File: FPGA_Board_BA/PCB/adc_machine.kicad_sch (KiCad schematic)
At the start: 15 parts, among them U11 LTC2320-16_CMOS

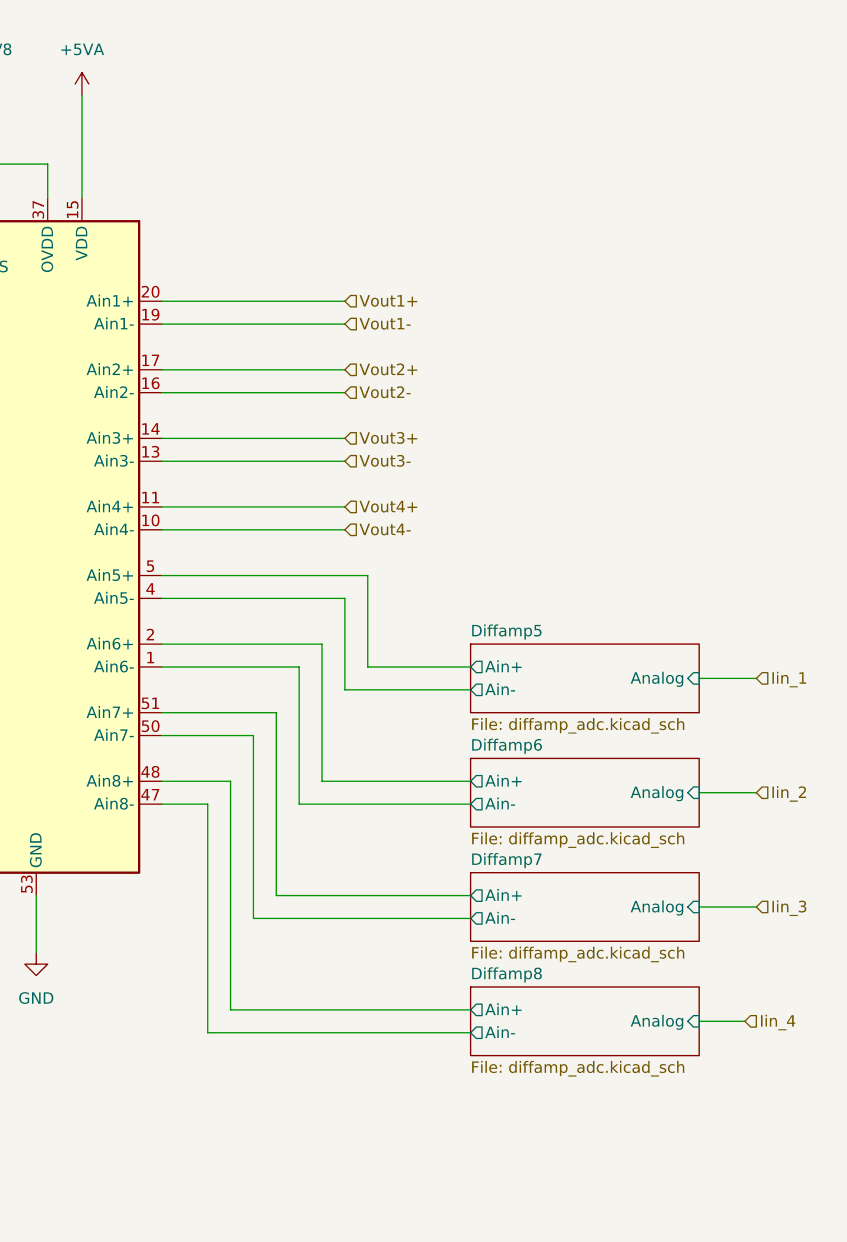
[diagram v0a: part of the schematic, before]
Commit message: started power DCDC layout
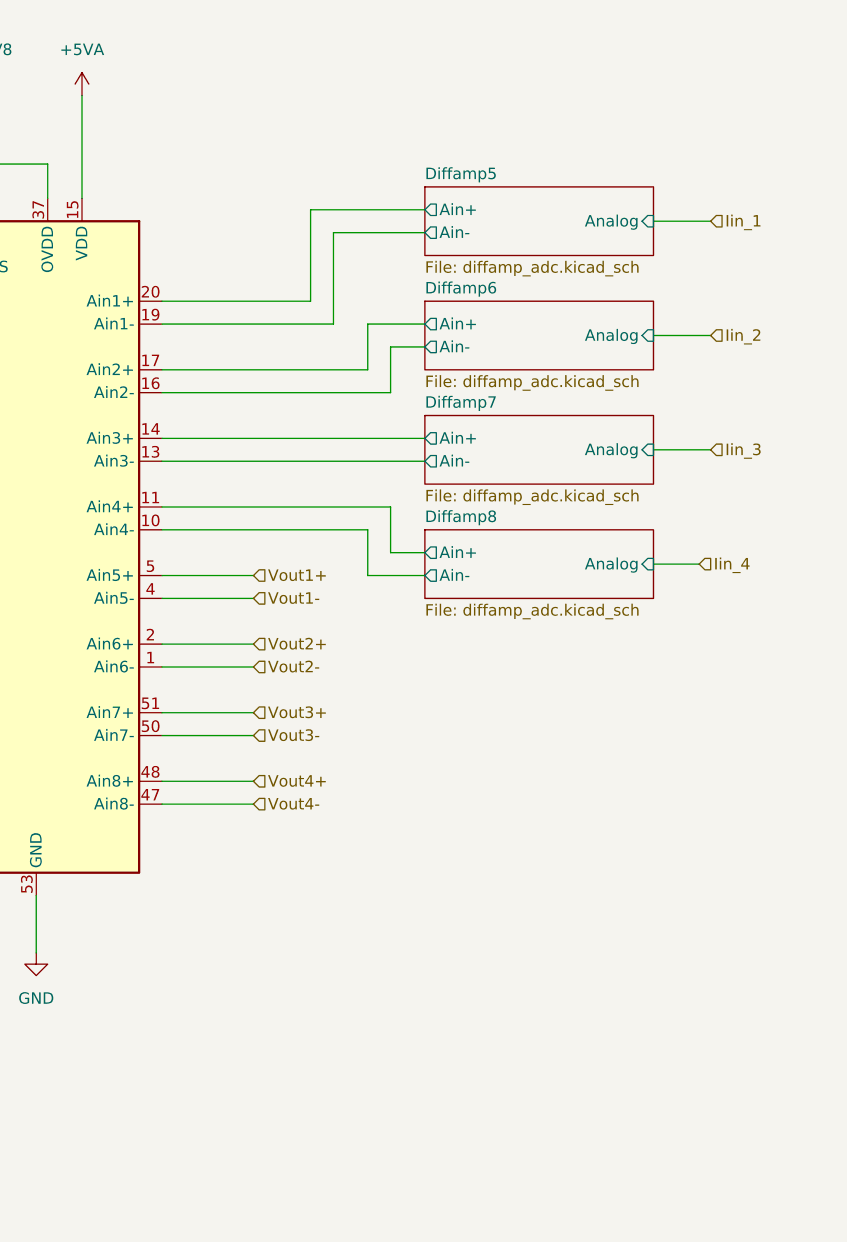
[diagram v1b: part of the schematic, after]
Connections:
- net Diffamp5/Ain+: now also U11.20 (Ain1+); no longer U11.5 (Ain5+)
- net Diffamp5/Ain-: now also U11.19 (Ain1-); no longer U11.4 (Ain5-)
- net Diffamp6/Ain+: now also U11.17 (Ain2+); no longer U11.2 (Ain6+)
- net Diffamp6/Ain-: now also U11.16 (Ain2-); no longer U11.1 (Ain6-)
- net Diffamp7/Ain+: now also U11.14 (Ain3+); no longer U11.51 (Ain7+)
- net Diffamp7/Ain-: now also U11.13 (Ain3-); no longer U11.50 (Ain7-)
- net Diffamp8/Ain+: now also U11.11 (Ain4+); no longer U11.48 (Ain8+)
- net Diffamp8/Ain-: now also U11.10 (Ain4-); no longer U11.47 (Ain8-)
- net Vout1+: now also U11.5 (Ain5+); no longer U11.20 (Ain1+)
- net Vout1-: now also U11.4 (Ain5-); no longer U11.19 (Ain1-)
- net Vout2+: now also U11.2 (Ain6+); no longer U11.17 (Ain2+)
- net Vout2-: now also U11.1 (Ain6-); no longer U11.16 (Ain2-)
- net Vout3+: now also U11.51 (Ain7+); no longer U11.14 (Ain3+)
- net Vout3-: now also U11.50 (Ain7-); no longer U11.13 (Ain3-)
- net Vout4+: now also U11.48 (Ain8+); no longer U11.11 (Ain4+)
- net Vout4-: now also U11.47 (Ain8-); no longer U11.10 (Ain4-)

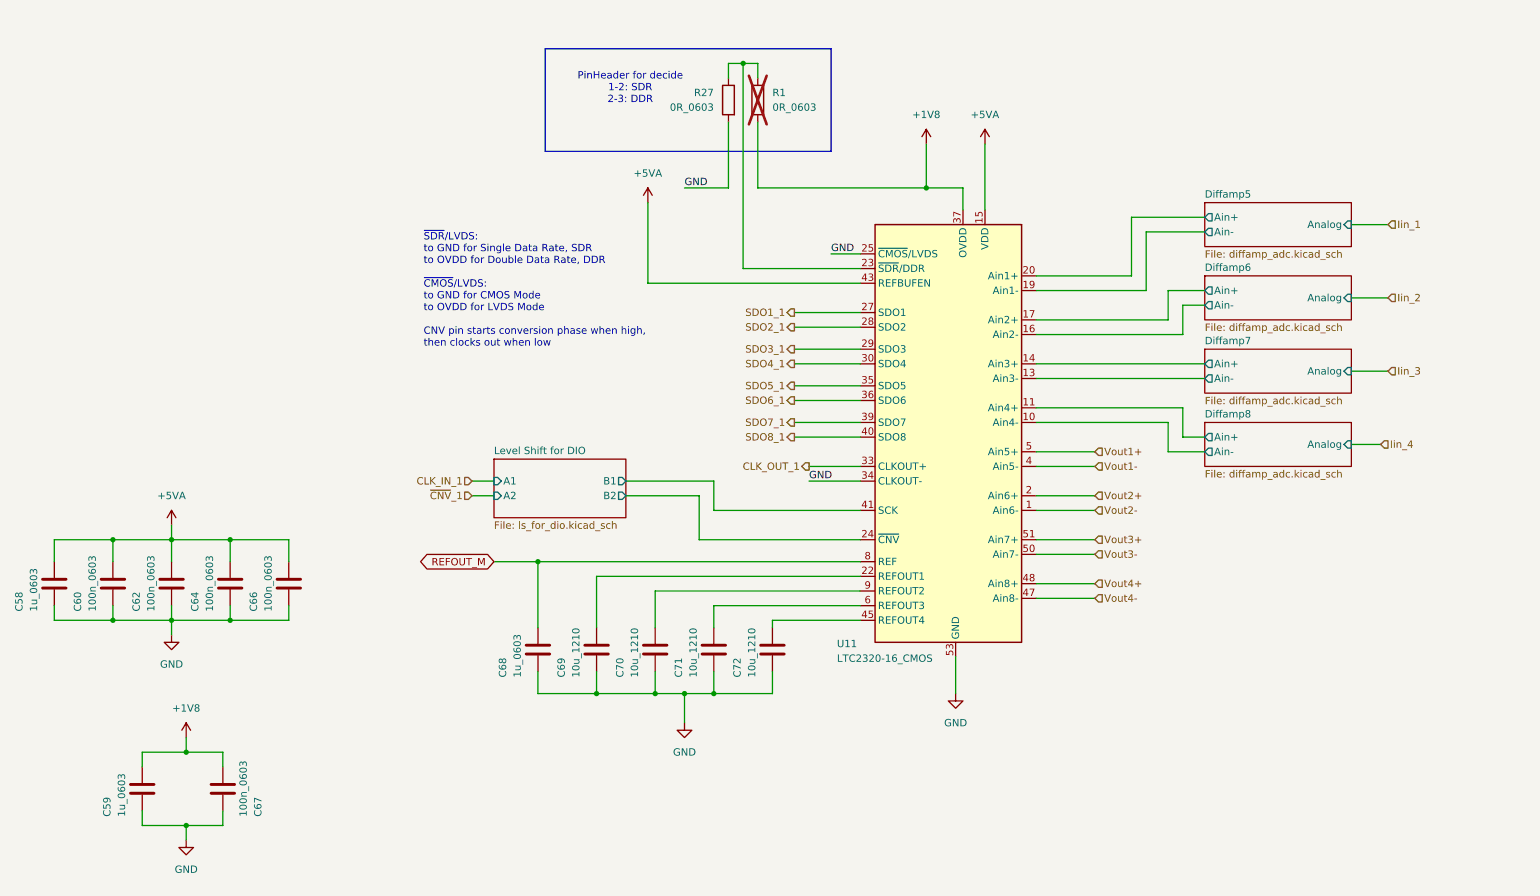
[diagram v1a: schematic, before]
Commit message: big schematic cleanup. Added wire to bus
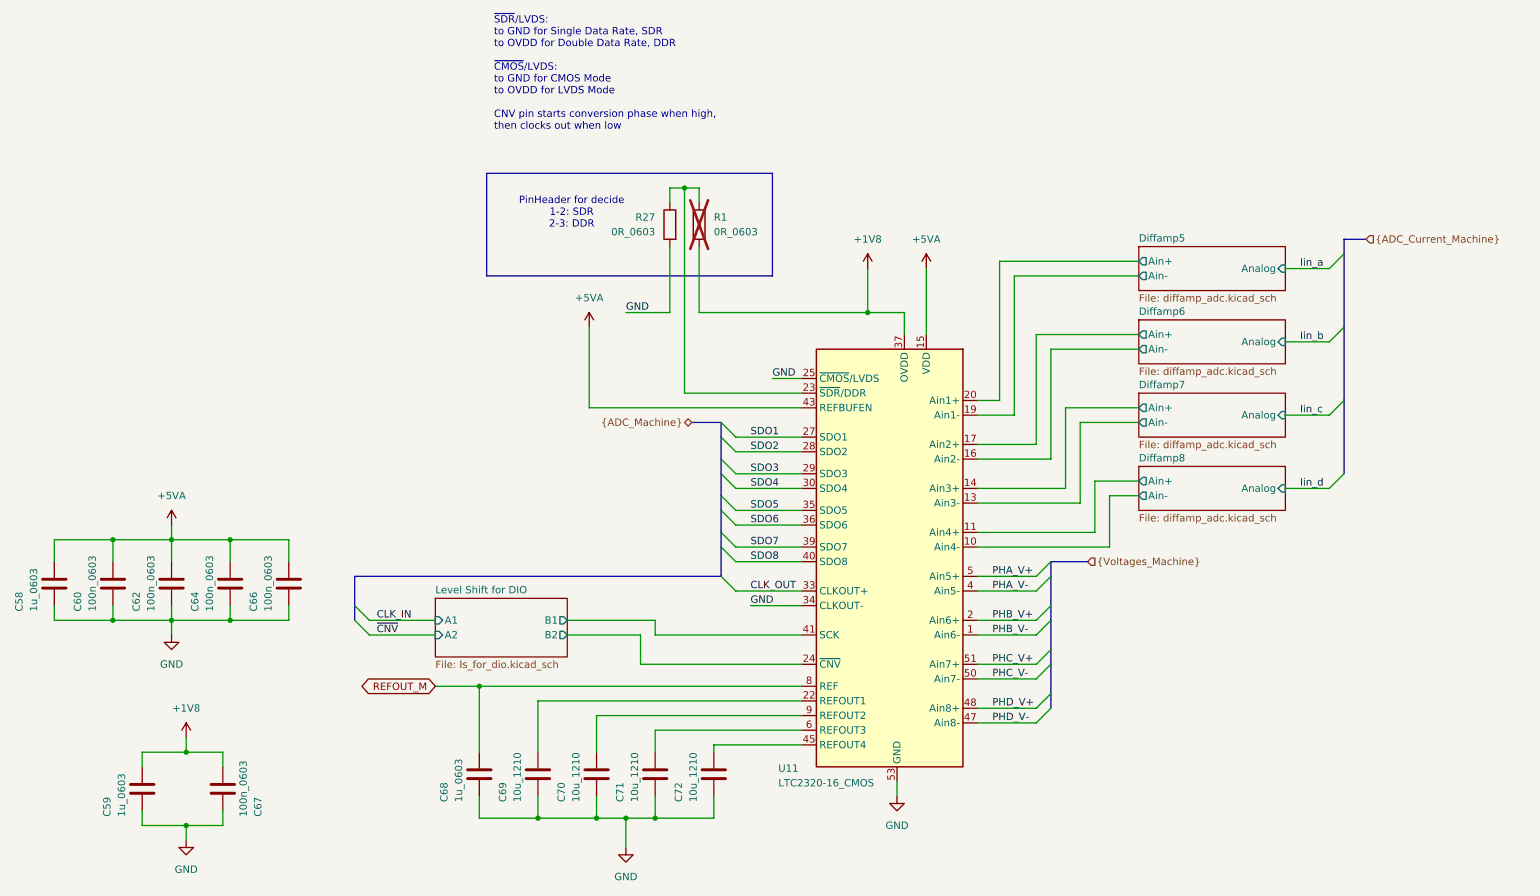
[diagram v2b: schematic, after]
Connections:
- net CLK_OUT_1 renamed CLK_OUT
- net SDO1_1 renamed SDO1
- net SDO2_1 renamed SDO2
- net SDO3_1 renamed SDO3
- net SDO4_1 renamed SDO4
- net SDO5_1 renamed SDO5
- net SDO6_1 renamed SDO6
- net SDO7_1 renamed SDO7
- net SDO8_1 renamed SDO8
- net Vout1+ renamed PHA_V+
- net Vout1- renamed PHA_V-
- net Vout2+ renamed PHB_V+
- net Vout2- renamed PHB_V-
- net Vout3+ renamed PHC_V+
- net Vout3- renamed PHC_V-
- net Vout4+ renamed PHD_V+
- net Vout4- renamed PHD_V-
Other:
- moved on the sheet: C68, C69, C70, C71, C72, R1, R27, U11

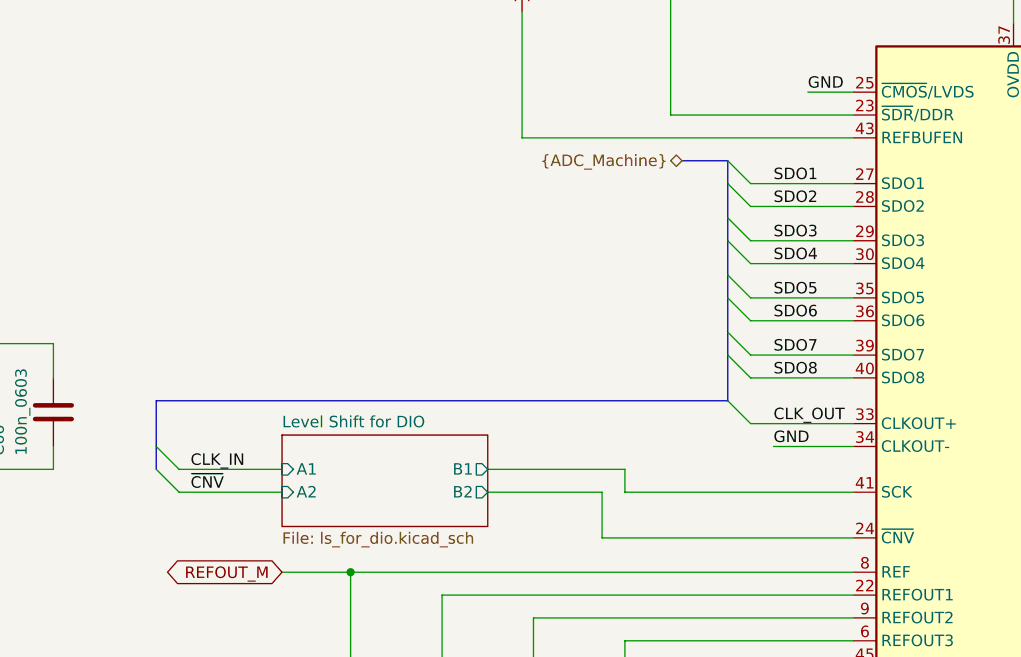
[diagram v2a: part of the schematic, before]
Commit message: PCB left side almost finished + some optimization in schematics
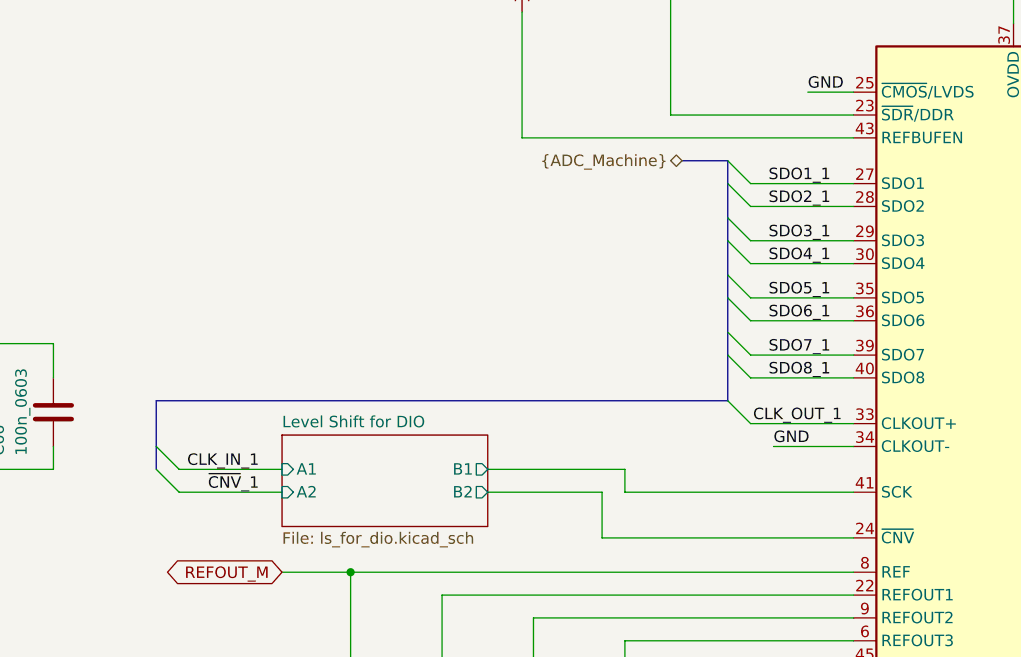
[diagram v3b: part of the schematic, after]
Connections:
- net CLK_OUT renamed CLK_OUT_1
- net SDO1 renamed SDO1_1
- net SDO2 renamed SDO2_1
- net SDO3 renamed SDO3_1
- net SDO4 renamed SDO4_1
- net SDO5 renamed SDO5_1
- net SDO6 renamed SDO6_1
- net SDO7 renamed SDO7_1
- net SDO8 renamed SDO8_1
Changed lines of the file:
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@@
 		)
 	)
-	(label "SDO4"
-		(at 152.4 101.6 0)
-		(effects
-			(font
-				(size 1.27 1.27)
-			)
-			(justify left bottom)
+	(label "~{CNV}_1"
+		(at 95.25 127 180)
+		(effects
+			(font
+				(size 1.27 1.27)
+			)
+			(justify right bottom)
+		)
+	)
+	(label "SDO4_1"
+		(at 158.75 101.6 180)
+		(effects
+			(font
+				(size 1.27 1.27)
+			)
+			(justify right bottom)
+		)
+	)
+	(label "CLK_IN_1"
+		(at 95.25 124.46 180)
+		(effects
+			(font
+				(size 1.27 1.27)
+			)
+			(justify right bottom)
 		)
 	)
@@
 		)
 	)
+	(label "SDO5_1"
+		(at 158.75 105.41 180)
+		(effects
+			(font
+				(size 1.27 1.27)
+			)
+			(justify right bottom)
+		)
+	)
 	(label "PHA_V+"
 		(at 194.31 116.84 0)
@@
 		)
 	)
+	(label "SDO8_1"
+		(at 158.75 114.3 180)
+		(effects
+			(font
+				(size 1.27 1.27)
+			)
+			(justify right bottom)
+		)
+	)
 	(label "PHD_V-"
 		(at 194.31 142.24 0)
@@
 		)
 	)
-	(label "SDO8"
-		(at 152.3999 114.3 0)
-		(effects
-			(font
-				(size 1.27 1.27)
-			)
-			(justify left bottom)
-		)
-	)
-	(label "~{CNV}"
-		(at 87.63 127 0)
-		(effects
-			(font
-				(size 1.27 1.27)
-			)
-			(justify left bottom)
-		)
-	)
 	(label "Iin_a"
 		(at 247.65 63.5 0)
@@
 		)
 	)
-	(label "SDO2"
-		(at 152.4 95.25 0)
-		(effects
-			(font
-				(size 1.27 1.27)
-			)
-			(justify left bottom)
-		)
-	)
-	(label "SDO7"
-		(at 152.4 111.76 0)
-		(effects
-			(font
-				(size 1.27 1.27)
-			)
-			(justify left bottom)
-		)
-	)
-	(label "SDO5"
-		(at 152.4 105.41 0)
-		(effects
-			(font
-				(size 1.27 1.27)
-			)
-			(justify left bottom)
-		)
-	)
-	(label "SDO3"
-		(at 152.4 99.06 0)
-		(effects
-			(font
-				(size 1.27 1.27)
-			)
-			(justify left bottom)
+	(label "SDO7_1"
+		(at 158.75 111.76 180)
+		(effects
+			(font
+				(size 1.27 1.27)
+			)
+			(justify right bottom)
 		)
 	)
@@
 		)
 	)
+	(label "SDO3_1"
+		(at 158.75 99.06 180)
+		(effects
+			(font
+				(size 1.27 1.27)
+			)
+			(justify right bottom)
+		)
+	)
 	(label "PHD_V+"
 		(at 194.31 139.7 0)
@@
 		)
 	)
-	(label "SDO6"
-		(at 152.4 107.95 0)
-		(effects
-			(font
-				(size 1.27 1.27)
-			)
-			(justify left bottom)
+	(label "SDO6_1"
+		(at 158.75 107.95 180)
+		(effects
+			(font
+				(size 1.27 1.27)
+			)
+			(justify right bottom)
+		)
+	)
+	(label "SDO1_1"
+		(at 158.75 92.71 180)
+		(effects
+			(font
+				(size 1.27 1.27)
+			)
+			(justify right bottom)
+		)
+	)
+	(label "CLK_OUT_1"
+		(at 160.02 119.38 180)
+		(effects
+			(font
+				(size 1.27 1.27)
+			)
+			(justify right bottom)
 		)
 	)
@@
 		)
 	)
-	(label "CLK_IN"
-		(at 87.63 124.46 0)
-		(effects
-			(font
-				(size 1.27 1.27)
-			)
-			(justify left bottom)
-		)
-	)
-	(label "SDO1"
-		(at 152.4 92.71 0)
-		(effects
-			(font
-				(size 1.27 1.27)
-			)
-			(justify left bottom)
-		)
-	)
-	(label "CLK_OUT"
-		(at 152.4 119.38 0)
-		(effects
-			(font
-				(size 1.27 1.27)
-			)
-			(justify left bottom)
-		)
-	)
+	(label "SDO2_1"
+		(at 158.75 95.25 180)
+		(effects
+			(font
+				(size 1.27 1.27)
+			)
+			(justify right bottom)
+		)
+	)

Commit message: optimised pinout in schematic + added level shifter for CLKOUT + got forward with layout
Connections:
- net CLK_OUT_1: no longer U11.33 (CLKOUT+)
- new net LS CLKOUT/A1: U11.33 (CLKOUT+)
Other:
- added sheet LS CLKOUT (ls_clkout.kicad_sch)
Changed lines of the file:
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@@
 	)
 	(bus_entry
-		(at 149.86 119.38)
+		(at 86.36 111.76)
 		(size -2.54 -2.54)
 		(stroke
@@
 		)
 	)
-	(bus
-		(pts
-			(xy 147.32 116.84) (xy 147.32 111.76)
-		)
-		(stroke
-			(width 0)
-			(type default)
-		)
-	)
 	(wire
 		(pts
@@
 	(wire
 		(pts
+			(xy 86.36 111.76) (xy 97.79 111.76)
+		)
+		(stroke
+			(width 0)
+			(type default)
+		)
+	)
+	(wire
+		(pts
 			(xy 135.89 124.46) (xy 135.89 127)
 		)
@@
 		)
 	)
+	(bus
+		(pts
+			(xy 83.82 109.22) (xy 83.82 121.92)
+		)
+		(stroke
+			(width 0)
+			(type default)
+		)
+	)
 	(wire
 		(pts
@@
 		)
 	)
+	(bus
+		(pts
+			(xy 140.97 111.76) (xy 147.32 111.76)
+		)
+		(stroke
+			(width 0)
+			(type default)
+		)
+	)
 	(wire
 		(pts
@@
 		)
 	)
+	(bus
+		(pts
+			(xy 83.82 102.87) (xy 83.82 109.22)
+		)
+		(stroke
+			(width 0)
+			(type default)
+		)
+	)
 	(wire
 		(pts
@@
 		)
 	)
+	(bus
+		(pts
+			(xy 140.97 111.76) (xy 140.97 102.87)
+		)
+		(stroke
+			(width 0)
+			(type default)
+		)
+	)
 	(wire
 		(pts
@@
 	(wire
 		(pts
-			(xy 149.86 119.38) (xy 161.29 119.38)
-		)
-		(stroke
-			(width 0)
-			(type default)
-		)
-	)
-	(wire
-		(pts
 			(xy 198.12 64.77) (xy 219.71 64.77)
 		)
@@
 		)
 	)
-	(bus
-		(pts
-			(xy 83.82 116.84) (xy 147.32 116.84)
-		)
-		(stroke
-			(width 0)
-			(type default)
-		)
-	)
 	(wire
 		(pts
@@
 	(wire
 		(pts
+			(xy 134.62 119.38) (xy 161.29 119.38)
+		)
+		(stroke
+			(width 0)
+			(type default)
+		)
+	)
+	(wire
+		(pts
 			(xy 52.07 124.46) (xy 62.23 124.46)
 		)
@@
 	(wire
 		(pts
+			(xy 134.62 111.76) (xy 120.65 111.76)
+		)
+		(stroke
+			(width 0)
+			(type default)
+		)
+	)
+	(wire
+		(pts
 			(xy 212.09 100.33) (xy 212.09 109.22)
 		)
@@
 	(wire
 		(pts
+			(xy 134.62 119.38) (xy 134.62 111.76)
+		)
+		(stroke
+			(width 0)
+			(type default)
+		)
+	)
+	(wire
+		(pts
 			(xy 52.07 110.49) (xy 62.23 110.49)
 		)
@@
 	(bus
 		(pts
-			(xy 204.47 137.16) (xy 204.47 132.08)
+			(xy 140.97 102.87) (xy 83.82 102.87)
 		)
 		(stroke
@@
 	(bus
 		(pts
-			(xy 147.32 102.87) (xy 147.32 99.06)
+			(xy 204.47 137.16) (xy 204.47 132.08)
 		)
 		(stroke
@@
 		)
 	)
-	(wire
+	(bus
 		(pts
-			(xy 149.86 114.3) (xy 161.29 114.3)
+			(xy 147.32 102.87) (xy 147.32 99.06)
 		)
 		(stroke
@@
 	(wire
 		(pts
-			(xy 149.86 95.25) (xy 161.29 95.25)
+			(xy 149.86 114.3) (xy 161.29 114.3)
 		)
 		(stroke
@@
 		)
 	)
-	(bus
+	(wire
 		(pts
-			(xy 83.82 121.92) (xy 83.82 116.84)
+			(xy 149.86 95.25) (xy 161.29 95.25)
 		)
 		(stroke
@@
 	)
 	(label "CLK_OUT_1"
-		(at 160.02 119.38 180)
+		(at 96.52 111.76 180)
 		(effects
 			(font
@@
 				)
 			)
+		)
+	)
+	(sheet
+		(at 97.79 107.95)
+		(size 22.86 7.62)
+		(exclude_from_sim no)
+		(in_bom yes)
+		(on_board yes)
+		(dnp no)
+		(fields_autoplaced yes)
+		(stroke
+			(width 0.1524)
+			(type solid)
+		)
+		(fill
+			(color 0 0 0 0.0000)
+		)
+		(property "Sheetname" "LS CLKOUT"
+			(at 97.79 107.2384 0)
+			(effects
+				(font
+					(size 1.27 1.27)
+				)
+				(justify left bottom)
+			)
+		)
+		(property "Sheetfile" "ls_clkout.kicad_sch"
+			(at 97.79 116.1546 0)
+			(effects
+				(font
+					(size 1.27 1.27)
+				)
+				(justify left top)
+			)
+		)
+		(pin "A1" input
+			(at 120.65 111.76 0)
+			(effects
+				(font
+					(size 1.27 1.27)
+				)
+				(justify right)
+			)
+		)
+		(pin "B1" output
+			(at 97.79 111.76 180)
+			(effects
+				(font
+					(size 1.27 1.27)
+				)
+				(justify left)
+			)
+		)
+		(instances
+			(project "FPGA_Board_BA"
+				(path "/fd7503bc-e7fc-4766-b224-3d1c3d7de5ff/61f82991-823e-4c29-9a78-9b2ec5b110b2"
+					(page "54")
+				)
+			)

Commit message: Nach meeting mit Leo
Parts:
- removed C69, C70, C71, C72: 10u_1210, WLIB_Capacitor:C_1210, symbol WLIB_C:10u_1210
- added C69, C70, C71, C72: 10u_0603, Capacitor_SMD:C_0603_1608Metric, symbol MYLIB_Misc:10u_0603
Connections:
- net GND: now also C69.1, C70.1, C71.1, C72.1
- net at U11.22 (REFOUT1): now also C69.2
- net at U11.45 (REFOUT4): now also C72.2
- net at U11.6 (REFOUT3): now also C71.2
- net at U11.9 (REFOUT2): now also C70.2
